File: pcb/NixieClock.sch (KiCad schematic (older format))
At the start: 40 parts, among them J1 USB_B, SW1 EG2219, SW2 SW_Push, SW3 SW_Push, SW4 SW_Push, SW5 SW_Push, SW6 SW_Push, SW7 SKQUCAA010, U1 DS3231, U2 PCF8574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

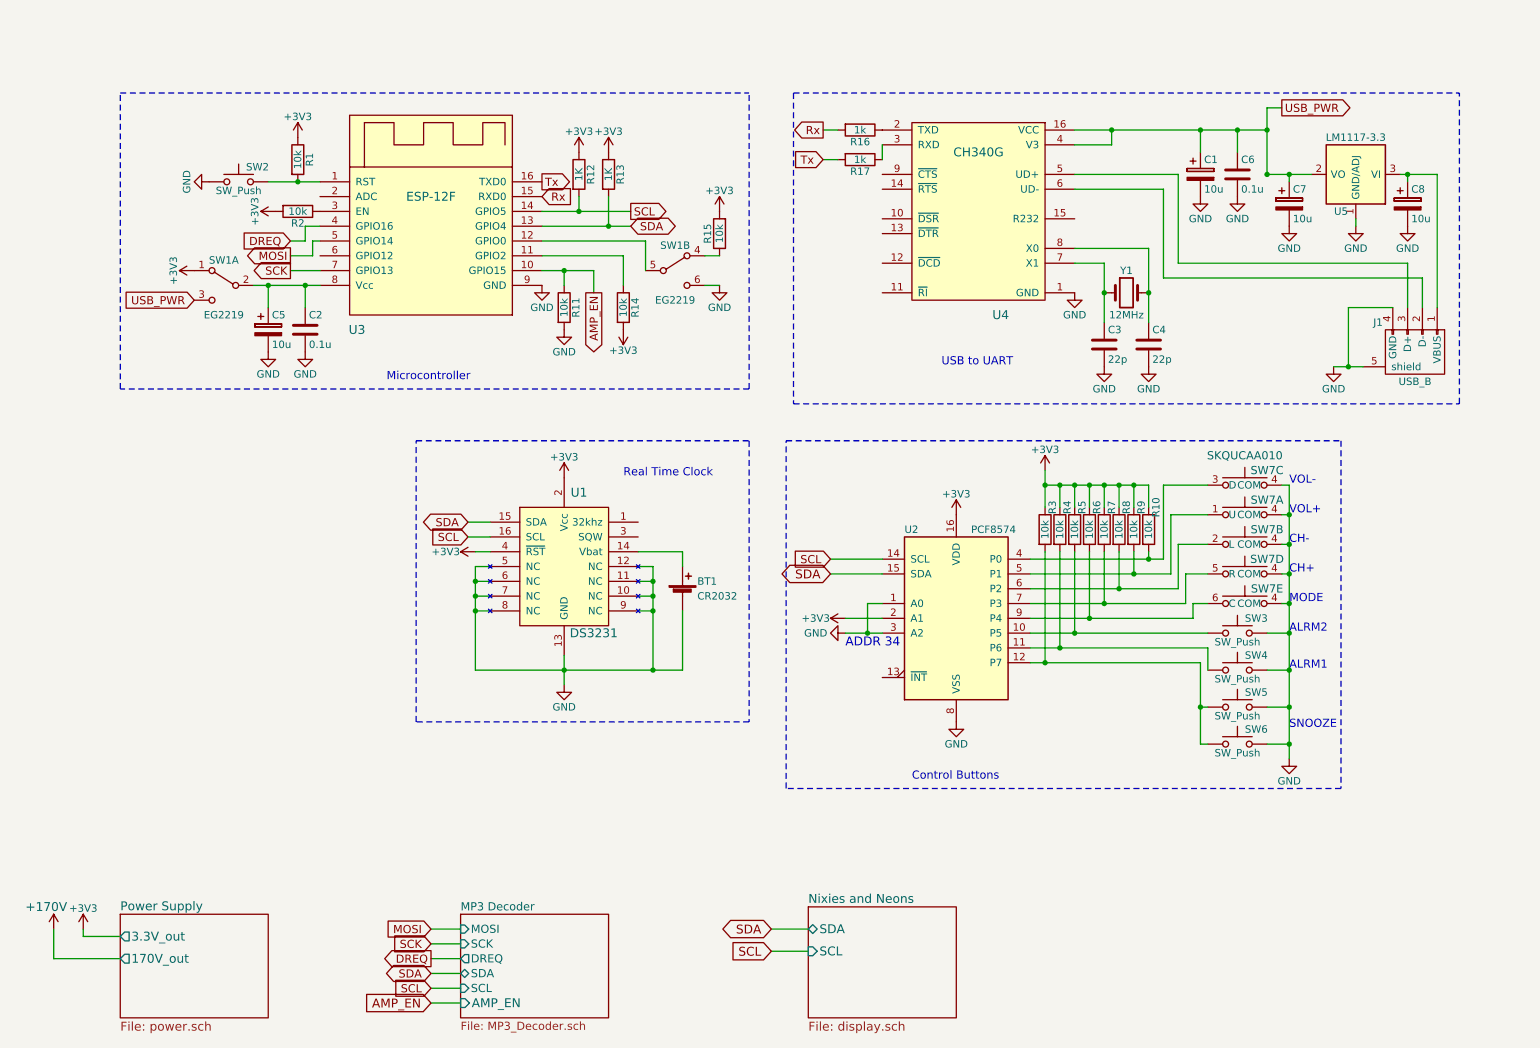
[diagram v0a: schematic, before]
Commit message: Use RTS and DTR for flashing instead of switch
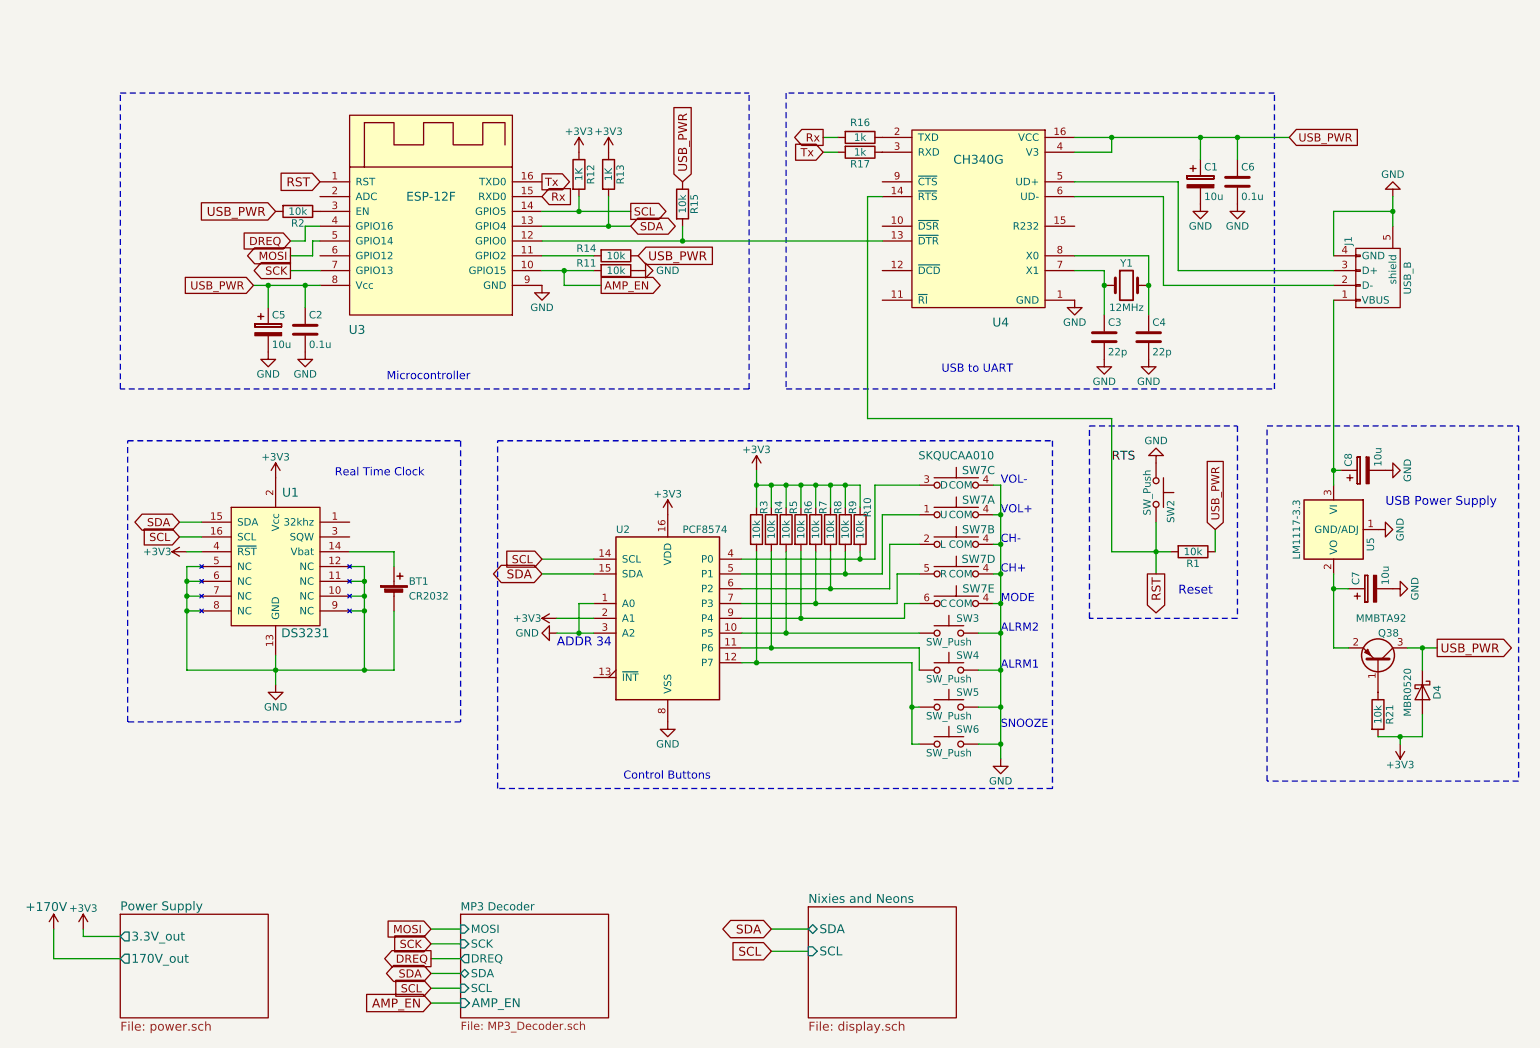
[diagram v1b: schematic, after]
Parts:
- removed SW1: EG2219, clock_footprints:EG2219, symbol SW_DPDT_x2
- added D4: MBR0520, Diodes_SMD:D_SOD-123, symbol D_Schottky
- added Q38: MMBTA92, TO_SOT_Packages_SMD:SOT-23_Handsoldering, symbol Q_PNP_BEC
- added R21: 10k, Resistors_SMD:R_0805_HandSoldering, symbol R
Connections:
- net +3V3: now also D4.2 (A), R21.2; no longer R1.1, R14.2, R15.2, R2.2
- net AMP_EN: now also R11.2; no longer R11.1
- net GND: now also R11.1; no longer R11.2
- net USB_PWR: now also C2.1, C5.1, R1.1, R14.1, R15.1, R2.2, U3.8 (Vcc), D4.1 (K), Q38.3 (C); no longer C7.1, U5.2 (VO), U5.4 (VO)
- net RST: now reaches R1.2, SW2.2, U3.1 (RST)
- net RST: now also U4.14 (~RTS)
- net at U3.11 (GPIO2): now also R14.2; no longer R14.1
- net at U3.12 (GPIO0): now also R15.2, U4.13 (~DTR)
- new net: C7.1, Q38.2 (E), U5.2 (VO), U5.4 (VO)
- new net: Q38.1 (B), R21.1
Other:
- note added: "Reset"
- note added: "USB Power Supply"
- moved on the sheet: BT1, C1, C3, C4, C6, C7, C8, J1, R1, R10, R11, R14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

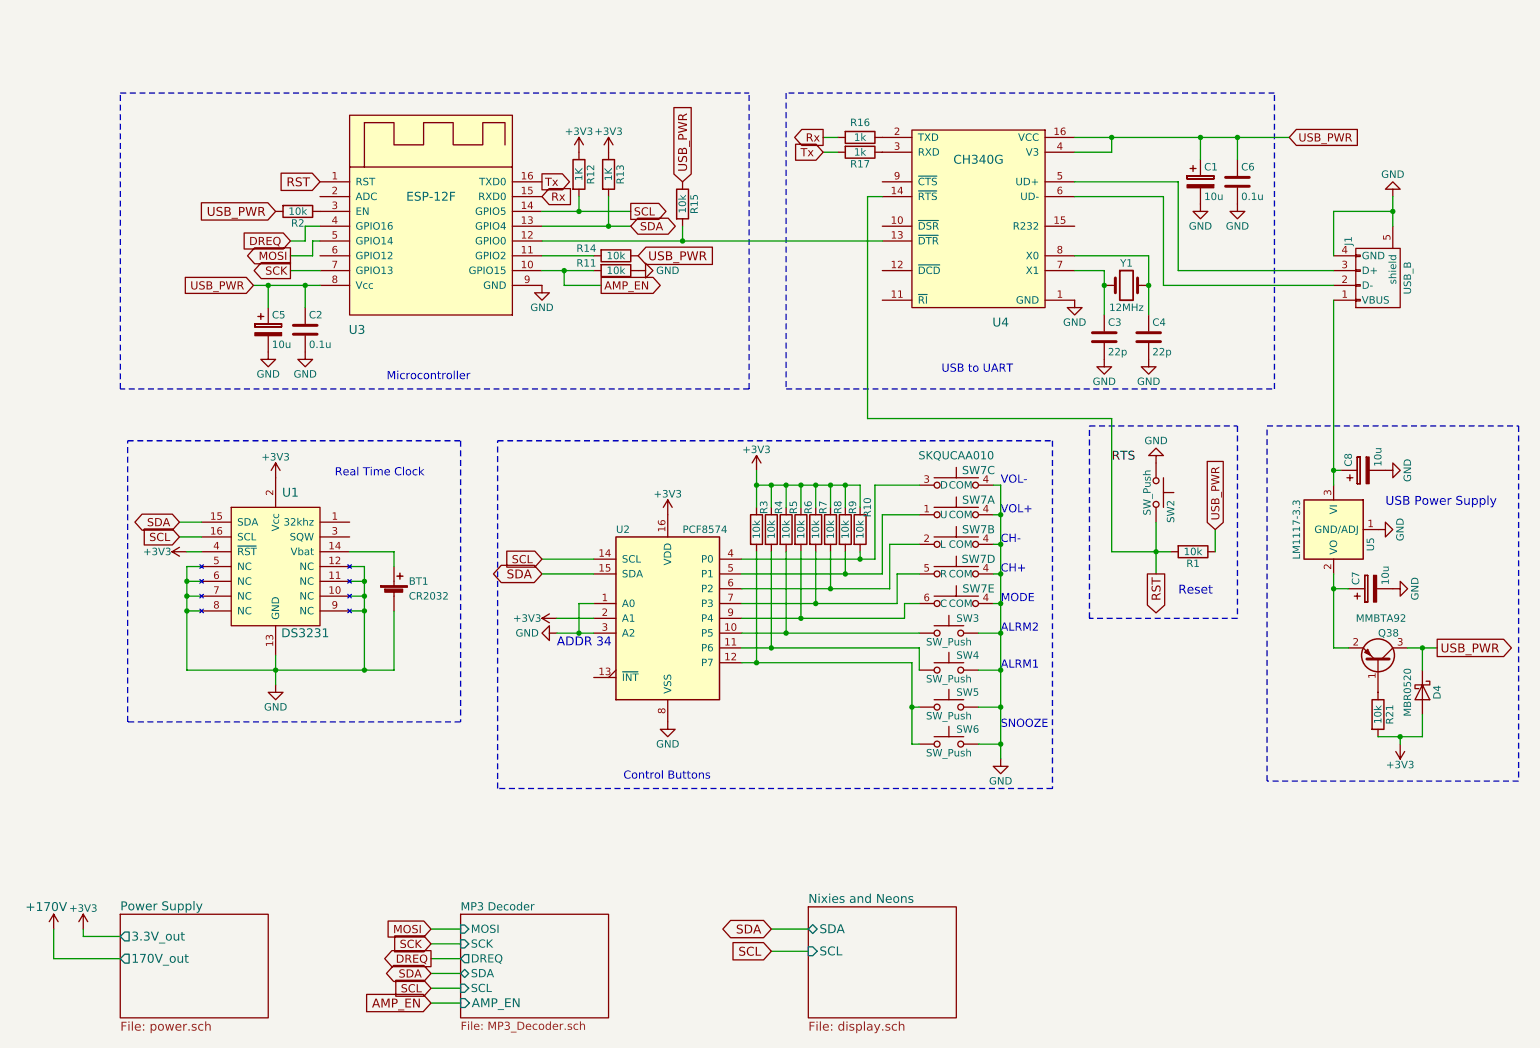
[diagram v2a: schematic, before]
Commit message: Switched to nodemcu-style flashing circuitry.
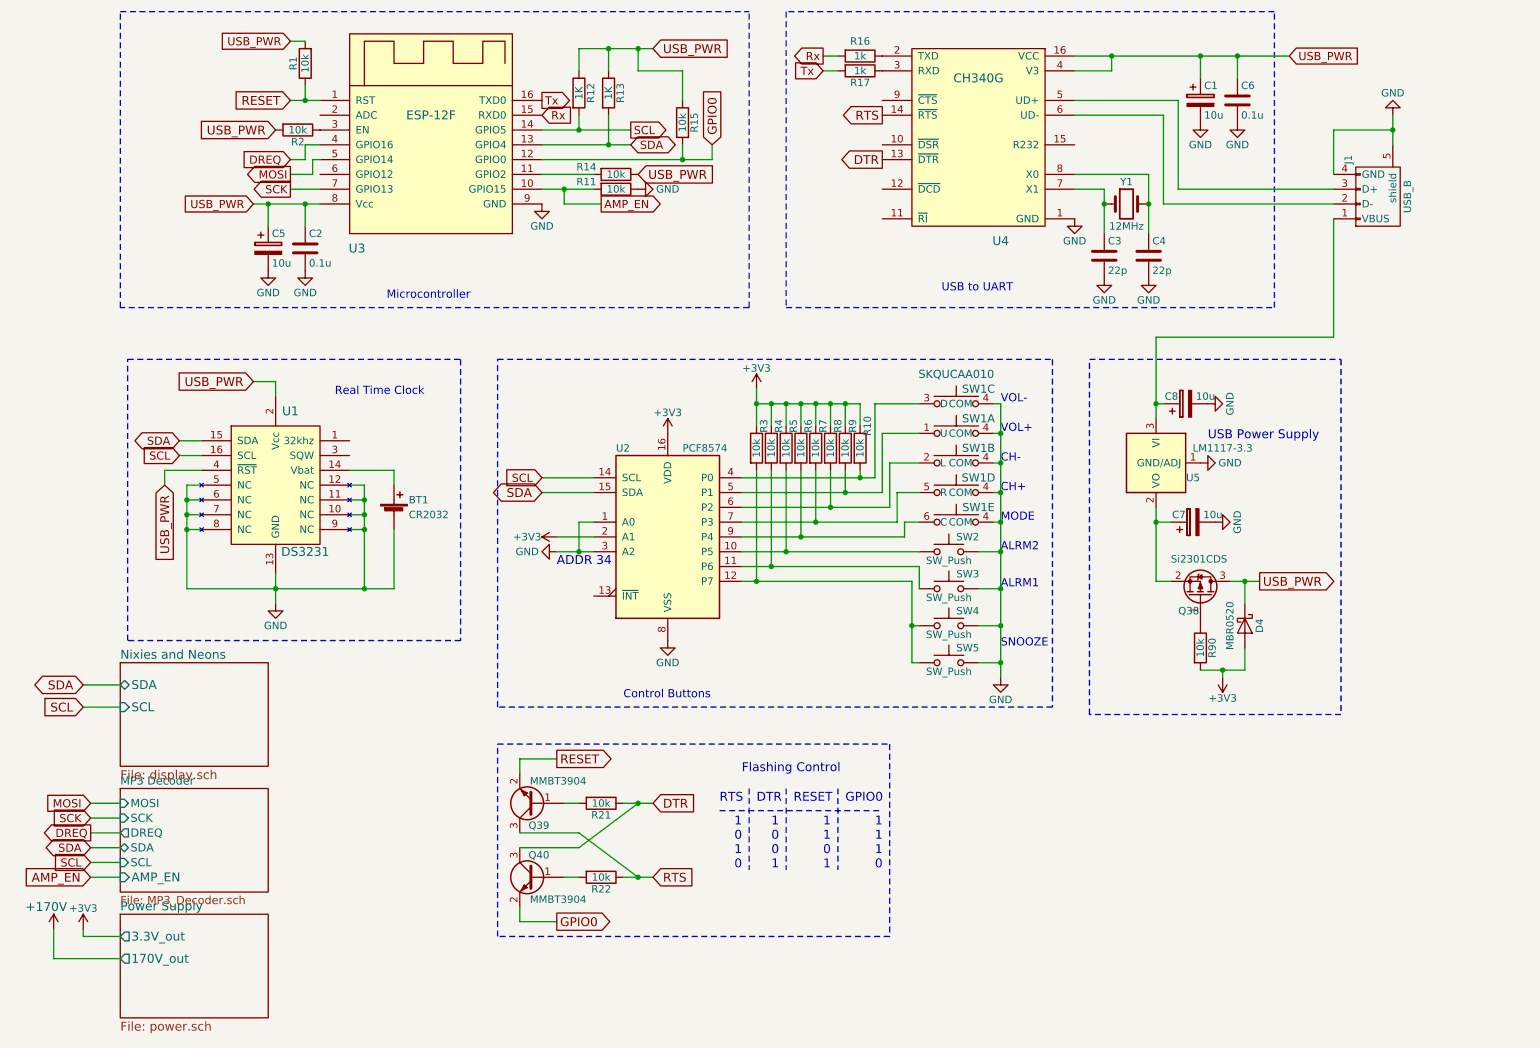
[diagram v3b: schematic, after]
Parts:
- removed Q38: MMBTA92, TO_SOT_Packages_SMD:SOT-23_Handsoldering, symbol Q_PNP_BEC
- removed SW2: SW_Push, Buttons_Switches_THT:SW_Tactile_SKHH_Angled, symbol SW_Push
- added Q38: Si2301CDS, TO_SOT_Packages_SMD:SOT-23_Handsoldering, symbol Q_PMOS_GSD
- added Q39, Q40: MMBT3904, TO_SOT_Packages_SMD:SOT-23_Handsoldering, symbol Q_NPN_BEC
- added R21, R22: 10k, Resistors_SMD:R_0805_HandSoldering, symbol R
- renumbered R21 to R90, SW7 to SW1, SW3 to SW2, SW4 to SW3, SW5 to SW4, SW6 to SW5
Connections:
- net +3V3: no longer R12.1, R13.1, U1.2 (Vcc), U1.4 (~RST)
- net USB_PWR: now also R1.2, R12.1, R13.1, U1.2 (Vcc), U1.4 (~RST), Q38.3 (D); no longer R1.1
- net GPIO0: now reaches R15.2, U3.12 (GPIO0)
- net GPIO0: now also Q40.2 (E); no longer U4.13 (~DTR)
- net at C7.1, U5.2 (VO), U5.4 (VO): now also Q38.2 (S)
- net at R90.1: now also Q38.1 (G)
- removed net RST: R1.2, U3.1 (RST), U4.14 (~RTS)
- new net: Q40.1 (B), R22.2
- new net: Q39.1 (B), R21.2
- new net DTR: Q40.3 (C), R21.1, U4.13 (~DTR)
- new net RESET: Q39.2 (E), R1.1, U3.1 (RST)
- new net RTS: Q39.3 (C), R22.1, U4.14 (~RTS)
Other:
- note added: "1\n0\n0\n1"
- note added: "1\n0\n1\n0"
- note added: "1\n1\n0\n1"
- note added: "1\n1\n1\n0"
- note added: "DTR"
- note added: "Flashing Control"
- note added: "GPIO0"
- note added: "RESET"
- note added: "RTS"
- note removed: "Reset"
- moved on the sheet: BT1, C1, C2, C3, C4, C5, C6, C7, C8, D4, J1, R1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
